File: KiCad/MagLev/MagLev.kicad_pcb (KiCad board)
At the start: 2 copper layers, 197 parts, among them J1 Barrel_Jack, J2 Programming header, J4 USB_B_Micro, Q1 ZX5T851GTA, Q10 ZX5T851GTA, Q12 AOD442G, Q13 AOD442G, Q14 ZX5T851GTA, Q16 TEMT7000X01, Q17 ZX5T851GTA, Q18 ZX5T1951GTA, Q2 ZX5T1951GTA, Q3 ZX5T851GTA, Q4 ZX5T1951GTA, Q5 ZX5T1951GTA, Q6 ZX5T851GTA, Q7 ZX5T1951GTA, Q8 ZX5T851GTA, Q9 ZX5T1951GTA, SW1 PTS645, U1 LM324, U10 X, U11 Y, U12 Z, U13 MCP1402, U14 MCP1402, U2 LM324, U3 L78L05_SO8, U4 TL431A, U5 LM393, U6 ATmega328P-A, U8 FT232RL, U9 LM1117MP-5.0, X1 L_Ferrite, X2 L_Ferrite, Y1 L_Ferrite, Y2 L_Ferrite, Y3 J49SMH-16MHz, Y5 L_Ferrite, Y6 L_Ferrite, Y8 L_Ferrite, Y9 L_Ferrite

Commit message: Place and route MCU page components.
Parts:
- added C18: 4.5n, Capacitor_SMD:C_0805_2012Metric_Pad1.18x1.45mm_HandSolder, F.Cu at (-97.8, 90.8)
- added C21: 4.5n, Capacitor_SMD:C_0805_2012Metric_Pad1.18x1.45mm_HandSolder, F.Cu at (-91.0, 90.8)
- added C26: 30n, Capacitor_SMD:C_0805_2012Metric_Pad1.18x1.45mm_HandSolder, F.Cu at (-97.8, 93.8)
- added C27: 30n, Capacitor_SMD:C_0805_2012Metric_Pad1.18x1.45mm_HandSolder, F.Cu at (-91.0, 93.8)
- added C28: 0.1uF, Capacitor_SMD:C_0805_2012Metric_Pad1.18x1.45mm_HandSolder, F.Cu at (143.9, 68.9)
- added H1: MountingHole_Pad, MountingHole:MountingHole_3.2mm_M3_Pad, F.Cu at (175.9, 45.1)
- added H2: MountingHole_Pad, MountingHole:MountingHole_3.2mm_M3_Pad, F.Cu at (128.9, 45.1)
- added H3: MountingHole_Pad, MountingHole:MountingHole_3.2mm_M3_Pad, F.Cu at (95.9, 78.1)
- added H4: MountingHole_Pad, MountingHole:MountingHole_3.2mm_M3_Pad, F.Cu at (95.9, 125.1)
- added H5: MountingHole_Pad, MountingHole:MountingHole_3.2mm_M3_Pad, F.Cu at (208.9, 78.1)
- added H6: MountingHole_Pad, MountingHole:MountingHole_3.2mm_M3_Pad, F.Cu at (208.9, 125.1)
- added H7: MountingHole_Pad, MountingHole:MountingHole_3.2mm_M3_Pad, F.Cu at (175.9, 158.1)
- added H8: MountingHole_Pad, MountingHole:MountingHole_3.2mm_M3_Pad, F.Cu at (128.9, 158.1)
- added NT1: NetTie_2, NetTie:NetTie-2_SMD_Pad2.0mm, F.Cu at (-96.1, 77.1)
- added NT2: NetTie_2, NetTie:NetTie-2_SMD_Pad2.0mm, F.Cu at (-96.1, 80.1)
- added NT3: NetTie_2, NetTie:NetTie-2_SMD_Pad0.5mm, F.Cu at (-98.3, 82.3)
- added R50: 1M, Resistor_SMD:R_0805_2012Metric_Pad1.20x1.40mm_HandSolder, F.Cu at (-91.0, 98.8)
- added R52: 1k, Resistor_SMD:R_0805_2012Metric_Pad1.20x1.40mm_HandSolder, F.Cu at (157.9, 58.1)
- added R53: 1k, Resistor_SMD:R_0805_2012Metric_Pad1.20x1.40mm_HandSolder, F.Cu at (160.4, 58.1)
- added R56: 1k, Resistor_SMD:R_0805_2012Metric_Pad1.20x1.40mm_HandSolder, F.Cu at (162.9, 58.1)
- added R64: 1k, Resistor_SMD:R_0805_2012Metric_Pad1.20x1.40mm_HandSolder, F.Cu at (165.4, 58.1)
- PB1, PB2, Q16: moved to B.Cu
- moved Q14 317.6 mm to (263.6, 133.9)
- moved R35 316.0 mm to (259.4, 145.1)
- moved D12 304.9 mm to (248.8, 98.6)
- moved D13 304.9 mm to (248.8, 101.6)
- moved D14 304.9 mm to (248.8, 104.6)
- moved D15 304.9 mm to (248.8, 107.7)
- moved D16 304.9 mm to (248.8, 110.7)
- moved D17 304.9 mm to (248.8, 113.8)
- moved D18 304.9 mm to (248.8, 116.8)
- moved D19 304.9 mm to (253.6, 98.6)
- moved D20 304.9 mm to (253.6, 101.6)
- moved D21 304.9 mm to (253.6, 104.6)
- moved D22 304.9 mm to (253.6, 107.7)
- moved D23 304.9 mm to (253.6, 110.7)
- moved D24 304.9 mm to (253.6, 113.8)
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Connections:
- C22 pad 2: GND -> Net-(C22-Pad2)
- C23 pad 2: GND -> Net-(C22-Pad2)
- D2 pad 2: GND -> GND1
- D30 pad 2: /MCU/PB3_MOSI -> Net-(J2-Pin_6)
- D30 pad 3: /MCU/PB4_MISO -> Net-(J2-Pin_5)
- D30 pad 4: /MCU/PB5_SCK -> Net-(J2-Pin_4)
- D32 pad 2: /MCU/RESET -> Net-(J2-Pin_3)
- D4 pad 2: GND -> GND1
- D6 pad 2: GND -> GND1
- D8 pad 2: GND -> GND1
- J1 pad 2: GND -> Net-(C22-Pad2)
- J1 pad 3: GND -> Net-(C22-Pad2)
- J2 pad 3: /MCU/RESET -> Net-(J2-Pin_3)
- J2 pad 4: /MCU/PB5_SCK -> Net-(J2-Pin_4)
- J2 pad 5: /MCU/PB4_MISO -> Net-(J2-Pin_5)
- J2 pad 6: /MCU/PB3_MOSI -> Net-(J2-Pin_6)
- J4 pad 6: Net-(J4-Shield) -> Earth
- Q12 pad 3: GND -> GND2
- Q13 pad 3: GND -> GND2
- Q2 pad 1: GND -> GND1
- Q4 pad 1: GND -> GND1
- Q7 pad 1: GND -> GND1
- Q9 pad 1: GND -> GND1
- R40 pad 1: GND -> /GNDcom
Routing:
- net Earth: track 0.00 -> 347.2 mm
- net +5V: track 0.00 -> 137.4 mm, vias 0 -> 2
- net /CoilPWM: track 0.00 -> 121.1 mm
- net Net-(D37-A): track 0.00 -> 119.4 mm, vias 0 -> 2
- net Net-(D38-A): track 0.00 -> 113.3 mm, vias 0 -> 2
- net /MCU/Touch1: track 0.00 -> 92.1 mm, vias 0 -> 3
- net VCC: track 4.49 -> 92.9 mm
- net /MCU/Touch2: track 0.00 -> 86.8 mm, vias 0 -> 3
- net /MCU/RESET: track 0.00 -> 68.9 mm, vias 0 -> 4
- net Net-(Y1-Pad2): track 75.5 -> 28.3 mm
- net Net-(X1-Pad2): track 72.1 -> 28.0 mm
- net /MCU/TXD0: track 0.00 -> 34.5 mm, vias 0 -> 4
- net /MCU/RXD0: track 0.00 -> 31.2 mm
- net /MCU/LED1: track 0.00 -> 27.6 mm
- net /MCU/LED2: track 0.00 -> 27.1 mm
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- added copper zone on F.Cu, net +5V
- added copper zone on B.Cu, net GND
- added copper zone on F.Cu, net VCC
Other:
- board outline added: 120 x 120 mm

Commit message: Place and route X and Y amplifier components.
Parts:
- removed TP1: CoilPWM, TestPoint:TestPoint_Pad_D2.0mm
- removed TP10: DR, TestPoint:TestPoint_Pad_D2.0mm
- removed TP11, TP12: Gc, TestPoint:TestPoint_Pad_D2.0mm
- removed TP13, TP14: Gx, TestPoint:TestPoint_Pad_D2.0mm
- removed TP15, TP16: Gy, TestPoint:TestPoint_Pad_D2.0mm
- removed TP17: LS, TestPoint:TestPoint_Pad_D2.0mm
- removed TP18: UV, TestPoint:TestPoint_Pad_D2.0mm
- removed TP19: WH, TestPoint:TestPoint_Pad_D2.0mm
- removed TP2: Vreg, TestPoint:TestPoint_Pad_D2.0mm
- removed TP20, TP21: Yin, TestPoint:TestPoint_Pad_D2.0mm
- removed TP22, TP23: Xin, TestPoint:TestPoint_Pad_D2.0mm
- removed TP3: Vref+, TestPoint:TestPoint_Pad_D2.0mm
- removed TP4: Vref-, TestPoint:TestPoint_Pad_D2.0mm
- removed TP5: En_sig, TestPoint:TestPoint_Pad_D2.0mm
- removed TP6: Vb_Zaxis, TestPoint:TestPoint_Pad_D2.0mm
- removed TP7: Hx, TestPoint:TestPoint_Pad_D2.0mm
- removed TP8: Hy, TestPoint:TestPoint_Pad_D2.0mm
- removed TP9: Vcc_en, TestPoint:TestPoint_Pad_D2.0mm
- moved C21 283.3 mm to (188.9, 134.9), turned to -135 degrees
- moved C27 274.8 mm to (179.3, 143.4), turned to 45 degrees
- moved Q2 250.7 mm to (195.2, 120.8)
- moved Q1 250.7 mm to (195.2, 113.2)
- moved Q6 250.1 mm to (194.7, 79.7)
- moved Q7 250.1 mm to (194.7, 86.9)
- moved C1 249.7 mm to (191.7, 137.7), turned to -135 degrees
- moved R9 240.3 mm to (195.4, 127.4), turned to 90 degrees
- moved C25 237.8 mm to (179.5, 135.7), turned to -45 degrees
- moved R34 235.2 mm to (195.4, 131.4), turned to -90 degrees
- moved R5 231.6 mm to (187.5, 133.4), turned to 45 degrees
- moved R8 230.4 mm to (186.0, 132.0), turned to 45 degrees
- moved R22 229.7 mm to (190.3, 136.3), turned to 45 degrees
- moved RV1 229.0 mm to (200.8, 129.4), turned to 180 degrees
- moved R6 228.9 mm to (184.6, 130.6), turned to 45 degrees
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- renumbered SW1 to RESET1
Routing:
- net Net-(Q6-B): track 0.00 -> 168.6 mm, vias 0 -> 2
- net Net-(Q3-B): track 0.00 -> 137.3 mm, vias 0 -> 4
- net /Y2: track 0.00 -> 116.7 mm
- net Net-(D37-A): track 119.4 -> 7.68 mm, vias 2 -> 0
- net Net-(D38-A): track 113.3 -> 9.73 mm, vias 2 -> 0
- net /X2: track 0.00 -> 79.2 mm, vias 0 -> 2
- net /CoilPWM: track 121.1 -> 45.2 mm
- net /MCU/Touch1: track 92.1 -> 18.6 mm
- net /X1: track 0.00 -> 66.7 mm
- net /MCU/Touch2: track 86.8 -> 23.7 mm
- net /DR: track 0.00 -> 61.7 mm, vias 0 -> 2
- net Net-(U2B-+): track 0.00 -> 59.4 mm, vias 0 -> 2
- net GND1: track 0.00 -> 56.3 mm
- net /Vref-: track 0.00 -> 53.2 mm
- net Net-(U1B-+): track 0.00 -> 49.8 mm, vias 0 -> 2
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- added copper zone on F.Cu, net Earth
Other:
- board text added: "PB3_MOSI PB4_MISO PB5_SCK RST +5V GND"
- board text added: "RX"
- board text added: "TX"

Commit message: Finish layout up to TPs.
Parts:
- removed NT1, NT2: NetTie_2, NetTie:NetTie-2_SMD_Pad2.0mm
- removed NT3: NetTie_2, NetTie:NetTie-2_SMD_Pad0.5mm
- removed Q17: ZX5T851GTA, Maglev_Footprint_Library:SOT-223-3_TabPin2_BJT
- added Q11: MMBT3904, Package_TO_SOT_SMD:SOT-23, F.Cu at (180.5, 81.0)
- added TP1: CoilPWM, TestPoint:TestPoint_Pad_D2.0mm, F.Cu at (1.52, 1.52)
- added TP10: DR, TestPoint:TestPoint_Pad_D2.0mm, F.Cu at (5.58, 17.7)
- added TP11: Gc, TestPoint:TestPoint_Pad_D2.0mm, F.Cu at (16.8, 1.52)
- added TP12: Gc, TestPoint:TestPoint_Pad_D2.0mm, F.Cu at (22.8, 1.52)
- added TP13: Gx, TestPoint:TestPoint_Pad_D2.0mm, F.Cu at (16.8, 5.58)
- added TP14: Gx, TestPoint:TestPoint_Pad_D2.0mm, F.Cu at (22.8, 5.58)
- added TP15: Gy, TestPoint:TestPoint_Pad_D2.0mm, F.Cu at (16.8, 9.62)
- added TP16: Gy, TestPoint:TestPoint_Pad_D2.0mm, F.Cu at (22.8, 9.62)
- added TP17: LS, TestPoint:TestPoint_Pad_D2.0mm, F.Cu at (146.4, 86.3)
- added TP18: UV, TestPoint:TestPoint_Pad_D2.0mm, F.Cu at (152.3, 66.7)
- added TP19: WH, TestPoint:TestPoint_Pad_D2.0mm, F.Cu at (28.9, 9.62)
- added TP2: Vreg, TestPoint:TestPoint_Pad_D2.0mm, F.Cu at (1.52, 5.58)
- added TP20: Yin, TestPoint:TestPoint_Pad_D2.0mm, F.Cu at (16.8, 13.7)
- added TP21: Yin, TestPoint:TestPoint_Pad_D2.0mm, F.Cu at (22.8, 13.7)
- added TP22: Xin, TestPoint:TestPoint_Pad_D2.0mm, F.Cu at (16.8, 17.7)
- added TP23: Xin, TestPoint:TestPoint_Pad_D2.0mm, F.Cu at (22.8, 17.7)
- added TP3: Vref+, TestPoint:TestPoint_Pad_D2.0mm, F.Cu at (1.52, 9.62)
- added TP4: Vref-, TestPoint:TestPoint_Pad_D2.0mm, F.Cu at (1.52, 13.7)
- added TP5: En_sig, TestPoint:TestPoint_Pad_D2.0mm, F.Cu at (1.52, 17.7)
- added TP6: Vb_Zaxis, TestPoint:TestPoint_Pad_D2.0mm, F.Cu at (5.58, 1.52)
- added TP7: Hx, TestPoint:TestPoint_Pad_D2.0mm, F.Cu at (5.58, 5.58)
- added TP8: Hy, TestPoint:TestPoint_Pad_D2.0mm, F.Cu at (5.58, 9.62)
- added TP9: Vcc_en, TestPoint:TestPoint_Pad_D2.0mm, F.Cu at (5.58, 13.7)
- D12, D13, D14, D15, D16, D17, D18, D19, D20, D21, D22, D23, D24, D25, D26, D27: moved to B.Cu
- J1: value Barrel_Jack -> FC681465S; footprint Connector_BarrelJack:BarrelJack_Horizontal -> Maglev_Footprint_Library:BarrelJack_CLIFF_FC681465S_SMT_Horizontal_No_Holes
- J4: footprint Connector_USB:USB_Micro-B_Amphenol_10118193-0001LF_Horizontal -> Connector_USB:USB_Micro-B_Amphenol_10104110_Horizontal
- R40: value 1MEG -> 1k
- moved Q5 280.8 mm to (200.3, 104.0), turned to 180 degrees
- moved D10 275.1 mm to (193.4, 70.6), turned to 90 degrees
- moved Q18 274.5 mm to (200.3, 96.5), turned to 180 degrees
- moved R67 253.1 mm to (180.5, 86.1), turned to 180 degrees
- moved R66 253.0 mm to (180.5, 84.0), turned to 180 degrees
- moved U5 251.9 mm to (171.6, 108.8)
- moved R27 251.8 mm to (174.2, 112.7)
- moved R68 250.2 mm to (177.5, 85.5), turned to -90 degrees
- moved R15 247.1 mm to (165.0, 106.7)
- moved C5 245.3 mm to (154.2, 138.4)
- moved R14 243.7 mm to (157.0, 143.4), turned to 90 degrees
- moved R17 243.5 mm to (165.9, 103.7), turned to 90 degrees
- moved R16 243.2 mm to (165.0, 108.8), turned to 180 degrees
- moved C2 242.3 mm to (150.1, 138.4), turned to 180 degrees
- moved C23 242.2 mm to (171.0, 91.0), turned to 90 degrees
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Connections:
- C22 pad 2: Net-(C22-Pad2) -> GND
- C23 pad 2: Net-(C22-Pad2) -> GND
- D2 pad 2: GND1 -> GND
- D4 pad 2: GND1 -> GND
- D6 pad 2: GND1 -> GND
- D8 pad 2: GND1 -> GND
- J1 pad 2: Net-(C22-Pad2) -> GND
- J1 pad 3: Net-(C22-Pad2) -> GND
- Q12 pad 3: GND2 -> GND
- Q13 pad 3: GND2 -> GND
- Q2 pad 1: GND1 -> GND
- Q4 pad 1: GND1 -> GND
- Q7 pad 1: GND1 -> GND
- Q9 pad 1: GND1 -> GND
- R36 pad 2: Vcc -> VCC
- R37 pad 2: Vcc -> VCC
- R40 pad 1: /GNDcom -> Net-(Q11-B)
- R40 pad 2: Net-(J4-Shield) -> /En_sig
- R41 pad 2: Vcc -> VCC
- R42 pad 2: Vcc -> VCC
- R43 pad 2: Vcc -> VCC
- R44 pad 2: Vcc -> VCC
- R45 pad 2: Vcc -> VCC
- R46 pad 2: Vcc -> VCC
- R50 pad 1: Net-(C22-Pad2) -> GND
- U13 pad 1: unconnected-(U13-NC-Pad1) -> GND
- U14 pad 1: unconnected-(U14-NC-Pad1) -> GND
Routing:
- net Net-(D13-K): track 0.00 -> 283.4 mm, vias 0 -> 8
- net Net-(D21-K): track 0.00 -> 277.7 mm, vias 0 -> 9
- net VCC: track 92.9 -> 315.5 mm, vias 0 -> 3
- net /MCU/Touch2: track 23.7 -> 209.9 mm
- net Net-(D37-A): track 7.68 -> 153.1 mm, vias 0 -> 2
- net /MCU/Touch1: track 18.6 -> 161.3 mm
- net Net-(D38-A): track 9.73 -> 137.0 mm, vias 0 -> 2
- net /Vref-: track 53.2 -> 180.1 mm, vias 0 -> 8
- net /Vref+: track 33.2 -> 159.1 mm, vias 1 -> 7
- net /CoilPWM: track 45.2 -> 127.9 mm, vias 0 -> 2
- net /X1: track 66.7 -> 146.7 mm, vias 0 -> 4
- net /H1: track 0.00 -> 56.4 mm, vias 0 -> 2
- net GND1: track 56.3 -> 0.00 mm
- net /DR: track 61.7 -> 117.2 mm, vias 2 -> 4
- net Net-(Q18-B): track 0.00 -> 53.0 mm, vias 0 -> 2
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- added copper zone on F.Cu, net /DR
- added copper zone on F.Cu, net /Vcc_en
- added copper zone on F.Cu, net /Vref+
- added copper zone on F.Cu, net /Vref-
- added copper zone on F.Cu, net GND
- added copper zone on F.Cu, net Net-(Q12-G)
- added copper zone on F.Cu, net Net-(Q13-G)
- removed copper zone on F.Cu, net Earth

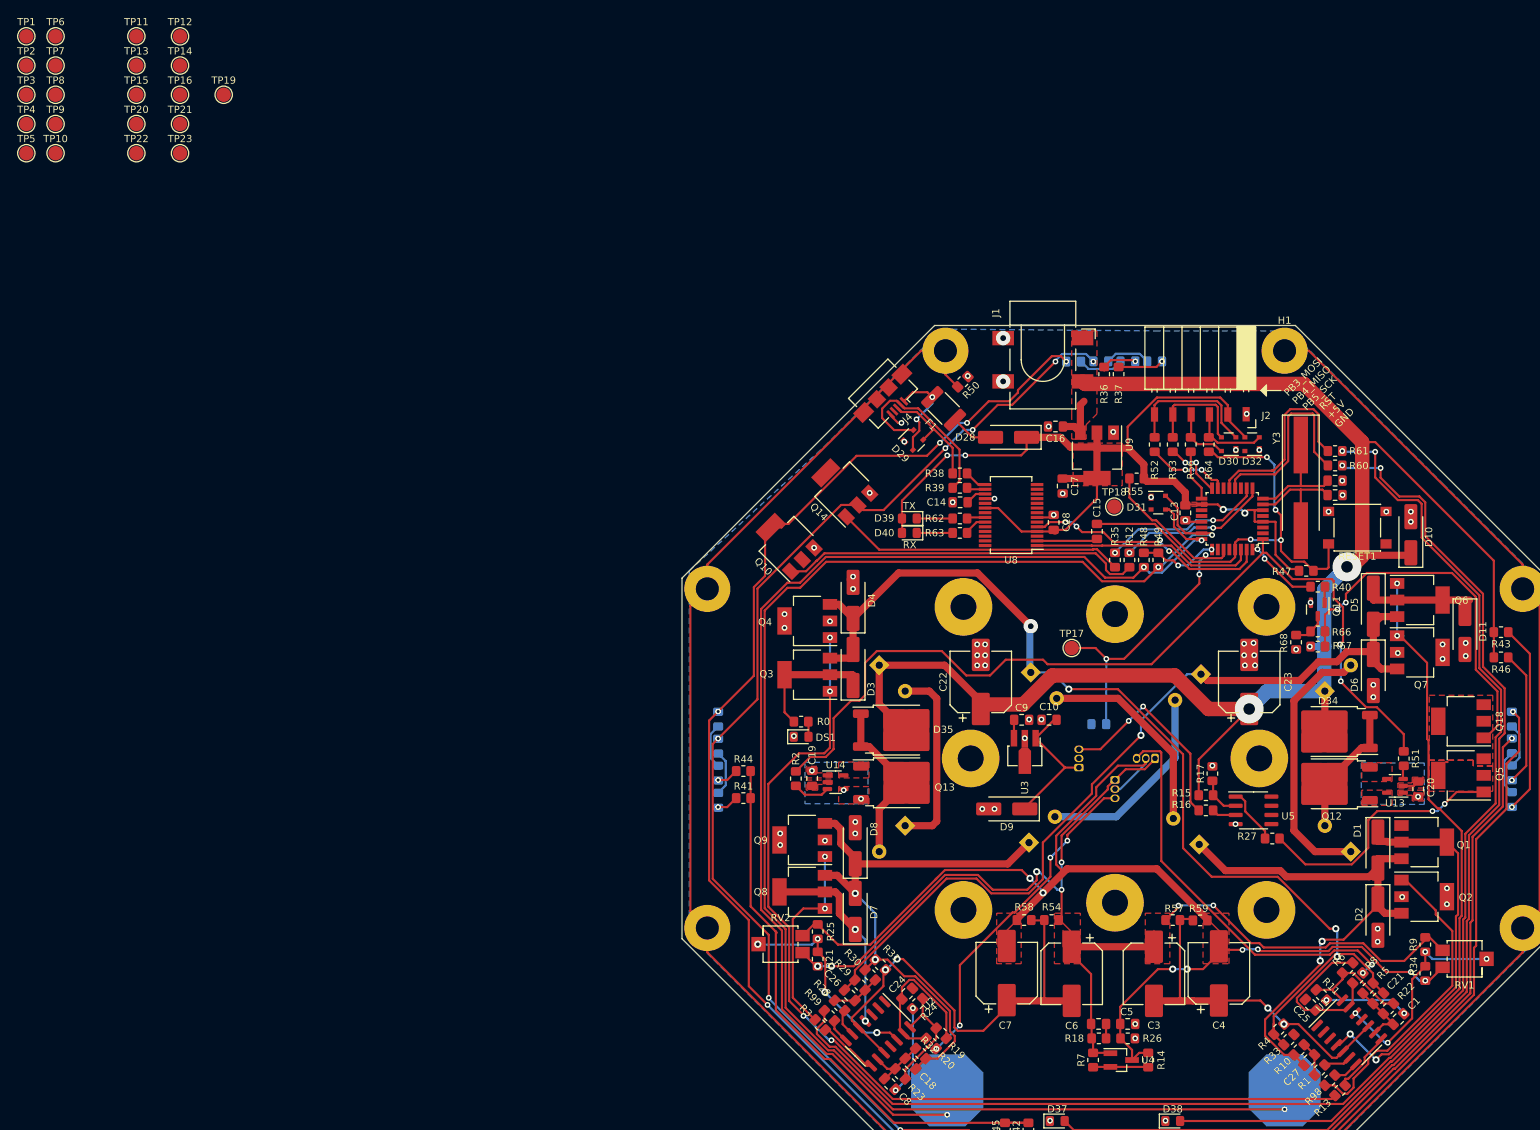
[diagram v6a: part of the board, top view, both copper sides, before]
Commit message: Route TPs, increase power trace size.
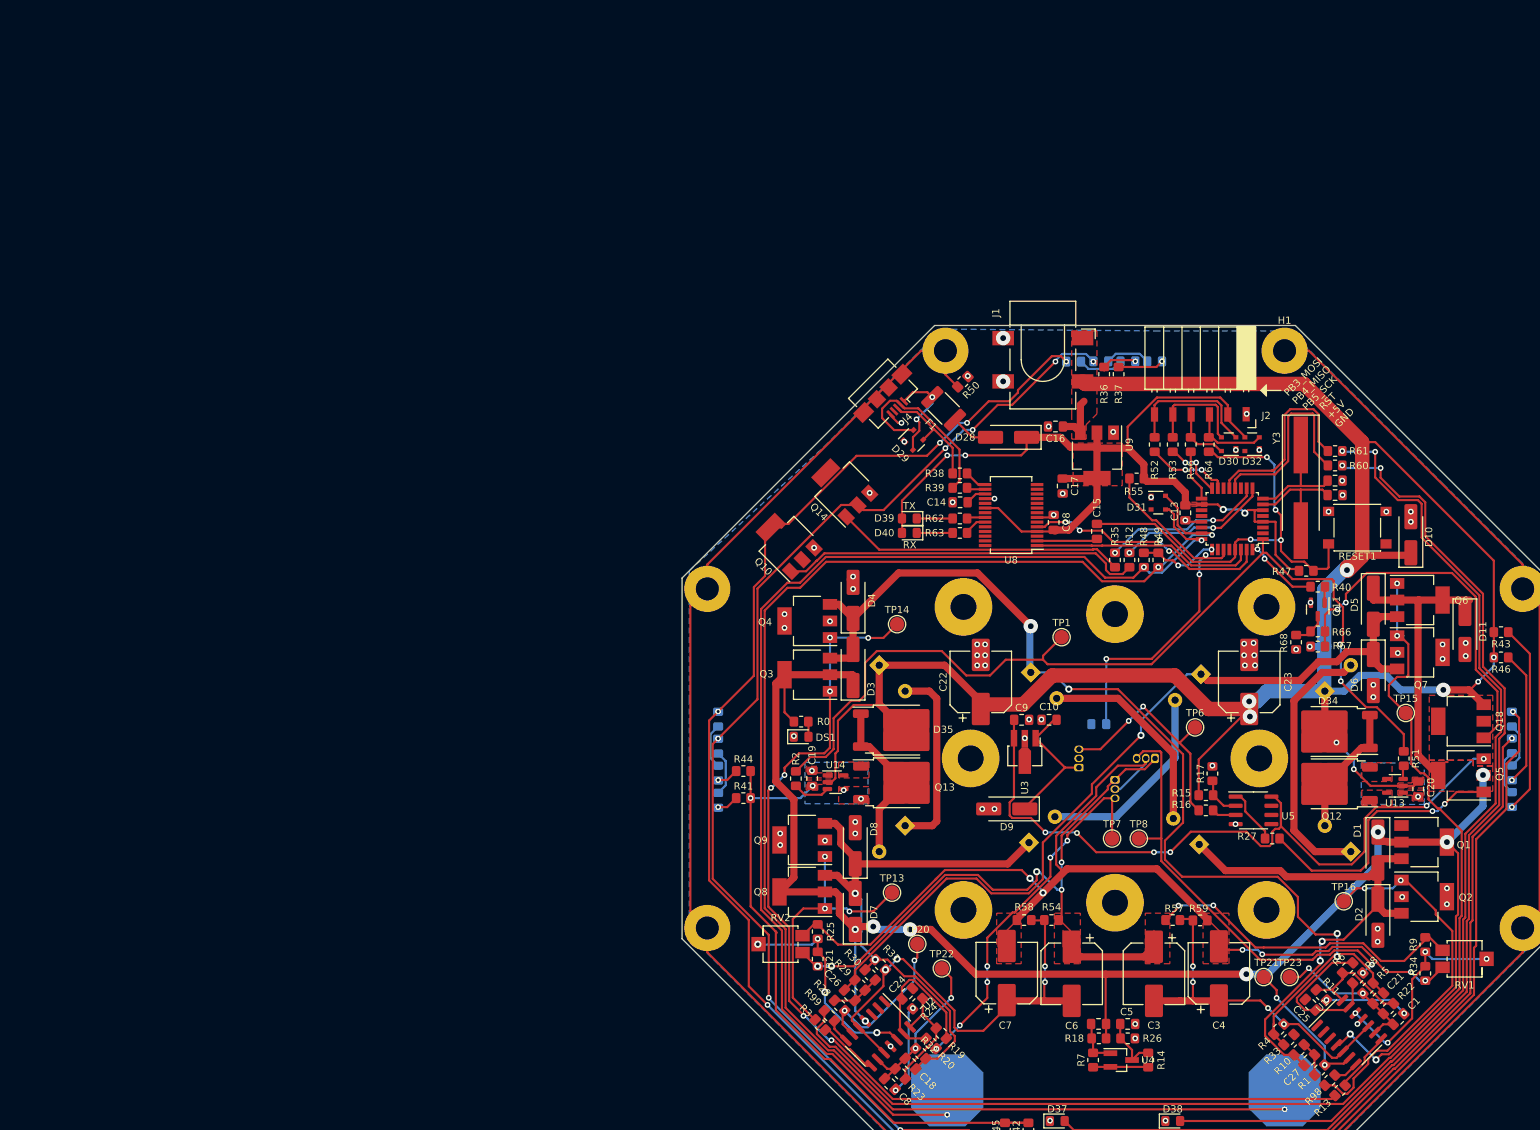
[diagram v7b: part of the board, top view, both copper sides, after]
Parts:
- removed TP10: DR, TestPoint:TestPoint_Pad_D2.0mm
- removed TP11, TP12: Gc, TestPoint:TestPoint_Pad_D2.0mm
- removed TP17: LS, TestPoint:TestPoint_Pad_D2.0mm
- removed TP18: UV, TestPoint:TestPoint_Pad_D2.0mm
- removed TP19: WH, TestPoint:TestPoint_Pad_D2.0mm
- removed TP2: Vreg, TestPoint:TestPoint_Pad_D2.0mm
- removed TP3: Vref+, TestPoint:TestPoint_Pad_D2.0mm
- removed TP4: Vref-, TestPoint:TestPoint_Pad_D2.0mm
- removed TP5: En_sig, TestPoint:TestPoint_Pad_D2.0mm
- removed TP9: Vcc_en, TestPoint:TestPoint_Pad_D2.0mm
- TP6: value Vb_Zaxis -> Hz
- moved TP16 196.2 mm to (184.1, 121.4)
- moved TP15 195.7 mm to (192.7, 95.3)
- moved TP23 191.5 mm to (176.6, 131.9)
- moved TP21 191.1 mm to (173.0, 131.9)
- moved TP6 184.7 mm to (163.5, 97.3)
- moved TP8 182.1 mm to (155.7, 112.7)
- moved TP7 181.4 mm to (152.0, 112.7)
- moved TP1 165.9 mm to (145.0, 84.8)
- moved TP22 158.8 mm to (128.4, 130.7)
- moved TP20 156.9 mm to (125.0, 127.3)
- moved TP13 155.3 mm to (121.5, 120.2)
- moved TP14 126.0 mm to (122.2, 83.0)
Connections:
- C2 pad 2: /Vref+ -> Net-(U4-C)
- C5 pad 1: /Vref- -> Net-(U4-A)
- R14 pad 2: /Vref- -> Net-(U4-A)
- R18 pad 1: /Vref+ -> Net-(U4-C)
- R26 pad 2: /Vref- -> Net-(U4-A)
- R7 pad 2: /Vref+ -> Net-(U4-C)
- TP1 pad 1: unconnected-(TP1-Pad1) -> /CoilPWM
- TP13 pad 1: Net-(R3-Pad2) -> Net-(Q8-B)
- TP14 pad 1: Net-(R13-Pad2) -> Net-(Q3-B)
- TP15 pad 1: Net-(R99-Pad2) -> Net-(Q6-B)
- TP16 pad 1: Net-(R98-Pad2) -> Net-(Q1-B)
- TP6 pad 1: unconnected-(TP6-Pad1) -> Net-(U12-OUTPUT)
- TP7 pad 1: unconnected-(TP7-Pad1) -> /H2
- TP8 pad 1: unconnected-(TP8-Pad1) -> /H1
- U4 pad 1: /Vref+ -> Net-(U4-C)
- U4 pad 3: /Vref- -> Net-(U4-A)
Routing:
- net /DR: track 117.2 -> 279.6 mm, vias 4 -> 10
- net /Vcc_en: track 2.56 -> 104.5 mm, vias 0 -> 6
- net VCC: track 315.5 -> 385.7 mm, vias 3 -> 11
- net /Vref-: track 180.1 -> 152.9 mm, vias 8 -> 6
- net Net-(U2B--): track 4.08 -> 22.6 mm, vias 0 -> 2
- net /Vref+: track 159.1 -> 143.0 mm
- net Net-(U1B--): track 3.85 -> 19.5 mm, vias 0 -> 2
- net Net-(U2C--): track 9.03 -> 22.7 mm, vias 0 -> 2
- net Net-(U1C--): track 9.32 -> 21.4 mm, vias 0 -> 2
- net Net-(Q8-B): track 27.7 -> 38.3 mm, vias 2 -> 3
- net Net-(Q3-B): track 138.7 -> 148.8 mm, vias 4 -> 7
- net Net-(Q1-B): track 43.4 -> 52.5 mm, vias 0 -> 2
- net Net-(U4-A): track 0.00 -> 8.33 mm
- net Net-(U4-C): track 0.00 -> 6.53 mm
- net /X1: track 146.7 -> 152.6 mm
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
